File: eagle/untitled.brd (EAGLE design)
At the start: 50 x 50 mm, 39 parts, among them J1 JTAG, Q1 16MHz, U1 MMA3202KEG

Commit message: Update eagle files.
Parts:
- added D10, D11, D12: DIODE, gipi:1206
- C1, C2, C3, C4, C5: device capacitor-wima:C2.5-2 -> SparkFun-Capacitors:1206
- moved GOLD_ORB_SM1 28.6 mm to (31.1, 56.5), flipped to the bottom
- moved C3 13.6 mm to (45.7, 78.1), turned to 0 degrees
- moved C5 10.0 mm to (38.7, 78.1), turned to 180 degrees
- moved JP5 8.28 mm to (5.08, 61.0)
- moved G1 5.46 mm to (8.89, 45.7), flipped to the bottom, turned to 0 degrees
- moved R1 5.08 mm to (12.7, 67.3)
- moved C6 1.91 mm to (12.7, 64.8)
- moved R2 0.63 mm to (12.7, 69.8)
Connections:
- new net N$32: D10.P$1, JP2.VBUS
- new net N$33: D11.P$1, G1.+@1, G1.+@2
- new net N$34: D12.P$1, JP5.2
- net N$28: now also D10.P$2, D11.P$2; no longer G1.+@1, G1.+@2, JP2.VBUS
- net VCC1: now also D12.P$2; no longer JP5.2
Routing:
- net VCC2: track 28.6 -> 59.3 mm, vias 2 -> 0
- net N$17: track 45.4 -> 75.8 mm, vias 2 -> 1
- net N$33: track 0.00 -> 23.4 mm, vias 0 -> 1
- net PD6: track 53.4 -> 34.4 mm, vias 1 -> 2
- net N$28: track 60.9 -> 46.5 mm
- net GND-ISO: track 75.4 -> 88.5 mm, vias 4 -> 9
- net N$11: track 11.0 -> 22.0 mm, vias 1 -> 0
- net PC7: track 63.0 -> 73.3 mm, vias 2 -> 1
- net PB6: track 67.9 -> 77.5 mm, vias 2 -> 1
- net N$13: track 5.90 -> 14.5 mm
- net N$12: track 9.19 -> 17.7 mm
- net N$5: track 16.7 -> 9.69 mm, vias 2 -> 0
- net N$34: track 0.00 -> 5.99 mm
- net N$32: track 0.00 -> 5.18 mm
- net N$6: track 15.3 -> 10.6 mm, vias 2 -> 0
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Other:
- board text added: "!RST"
- board text added: "GND"
- board text added: "PB1"
- board text added: "PB2"
- board text added: "PB3"
- board text added: "VCC"

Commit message: Update board layout.
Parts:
- added D9: (no value), SparkFun-LED:LED-1206
- added JP3: (no value), SparkFun-Connectors:1X04
- added R14: (no value), SparkFun-Passives:1206
- moved SJ1 2.01 mm to (29.8, 75.6)
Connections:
- new net N$18: D9.A, R14.2
- new net PB0: JP3.3, U$1.8
- new net PD0: JP3.1, U$1.18
- new net PD1: JP3.2, U$1.19
- new net PE6: JP3.4, U$1.1
- net GND-ISO: now also D9.C
- net N$28: now also R14.1
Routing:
- net PE6: track 0.00 -> 29.3 mm, vias 0 -> 1
- net PB0: track 0.00 -> 28.8 mm, vias 0 -> 1
- net PD0: track 0.00 -> 28.1 mm, vias 0 -> 1
- net PD1: track 0.00 -> 22.6 mm, vias 0 -> 1
- net GND-ISO: track 88.5 -> 67.3 mm, vias 9 -> 10
- net VCC1: track 76.5 -> 91.7 mm
- net VCC2: track 59.3 -> 48.0 mm
- net X: track 66.1 -> 70.5 mm, vias 0 -> 1
- net N$18: track 0.00 -> 4.38 mm
- net N$6: track 10.6 -> 13.3 mm
- net N$28: track 46.5 -> 49.3 mm
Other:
- board text added: "!CTS"
- board text added: "!RTS"
- board text added: "ACC"
- board text added: "ATMEGA"
- board text added: "PB0"
- board text added: "PD0"
- board text added: "PD1"
- board text added: "PE6"
- board text added: "PWR"
- board text added: "RX"
- board text added: "TX"

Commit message: Update eagle.
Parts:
- added U$2: KITTEN, gipi:KITTEN
- G1: device battery:10MM_SM_COIN_CELL_CLIP -> SparkFun-Electromechanical:BATTCOM_20MM_PTH
- moved G1 6.17 mm to (15.0, 45.1)
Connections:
- net GND-ISO: now also G1.1; no longer G1.-
- net N$33: now also G1.2; no longer G1.+@1, G1.+@2
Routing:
- net GND-ISO: track 67.3 -> 72.9 mm
- net N$33: track 23.4 -> 26.6 mm
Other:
- board text added: "+"
- board text added: "-"
- board text added: "github.com/gipi/pov-project"
- board text removed: "UP ->"
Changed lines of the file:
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@@
 <setting verticaltext="up"/>
 </settings>
-<grid distance="25" unitdist="mil" unit="mil" style="lines" multiple="1" display="no" altdistance="5" altunitdist="mil" altunit="mil"/>
+<grid distance="0.001667" unitdist="inch" unit="inch" style="lines" multiple="1" display="yes" altdistance="5" altunitdist="mil" altunit="mil"/>
 <layers>
 <layer number="1" name="Top" color="4" fill="1" visible="yes" active="yes"/>
@@
 <layer number="20" name="Dimension" color="15" fill="1" visible="yes" active="yes"/>
 <layer number="21" name="tPlace" color="7" fill="1" visible="yes" active="yes"/>
-<layer number="22" name="bPlace" color="7" fill="1" visible="yes" active="yes"/>
+<layer number="22" name="bPlace" color="15" fill="1" visible="yes" active="yes"/>
 <layer number="23" name="tOrigins" color="15" fill="1" visible="yes" active="yes"/>
 <layer number="24" name="bOrigins" color="15" fill="1" visible="yes" active="yes"/>
@@
 <wire x1="50" y1="80" x2="0" y2="80" width="0" layer="20"/>
 <wire x1="0" y1="80" x2="0" y2="30" width="0" layer="20"/>
-<text x="41.91" y="77.47" size="1.778" layer="21">UP -&gt;</text>
 <text x="44.704" y="31.369" size="0.8128" layer="21" font="vector">PD4</text>
 <text x="44.704" y="33.909" size="0.8128" layer="21" font="vector">PD6</text>
@@
 <text x="45.339" y="61.976" size="0.8128" layer="21" font="vector" ratio="10">PD1</text>
 <text x="49.149" y="62.484" size="0.8128" layer="21" font="vector" ratio="10" rot="R90">PD0</text>
+<text x="5.715" y="45.466" size="1.778" layer="21">-</text>
+<text x="20.955" y="45.085" size="1.778" layer="21">+</text>
+<circle x="6.35" y="46.355" radius="1.27" width="0.3048" layer="21"/>
+<text x="49.582246875" y="66.942384375" size="2.1844" layer="22" font="vector" rot="MR0">github.com/gipi/pov-project</text>
 </plain>
 <attributes>
@@
 <element name="C2" library="SparkFun-Capacitors" package="1206" value="" x="19.05" y="43.815"/>
 <element name="U1" library="gipi" package="SOIC20" value="MMA3202KEG" x="40.64" y="69.85"/>
-<element name="G1" library="battery" package="10MM_SM_COIN_CELL_CLIP" value="BAT" x="8.89" y="45.72" smashed="yes" rot="MR0">
-<attribute name="NAME" x="2.85375" y="48.44251875" size="1.27" layer="26" font="vector" rot="MR0"/>
-<attribute name="VALUE" x="13.37255" y="39.28065" size="1.27" layer="28" font="vector" rot="MR0"/>
+<element name="G1" library="SparkFun-Electromechanical" package="BATTCOM_20MM_PTH" value="BAT" x="15.025" y="45.085" smashed="yes" rot="MR0">
+<attribute name="NAME" x="8.98875" y="47.80751875" size="1.27" layer="26" font="vector" rot="MR0"/>
+<attribute name="VALUE" x="19.50755" y="38.64565" size="1.27" layer="28" font="vector" rot="MR0"/>
 </element>
 <element name="C3" library="SparkFun-Capacitors" package="1206" value="" x="45.72" y="78.105" smashed="yes">
-<attribute name="NAME" x="42.799" y="77.089" size="1.27" layer="25" ratio="10" rot="R90"/>
+<attribute name="NAME" x="49.53" y="77.089" size="1.27" layer="25" ratio="10" rot="R90"/>
 <attribute name="VALUE" x="44.069" y="75.311" size="1.27" layer="27" ratio="10"/>
 </element>
@@
 <element name="R14" library="SparkFun-Passives" package="1206" value="" x="18.415" y="69.85"/>
 <element name="JP3" library="SparkFun-Connectors" package="1X04" value="" x="48.26" y="60.325" rot="R180"/>
+<element name="U$2" library="gipi" package="KITTEN" value="KITTEN" x="47.4228125" y="32.7302125" rot="MR0"/>
 </elements>
 <signals>
@@
 <contactref element="C1" pad="1"/>
 <contactref element="C2" pad="1"/>
-<contactref element="G1" pad="-"/>
+<contactref element="G1" pad="1"/>
 <contactref element="C5" pad="1"/>
 <contactref element="C4" pad="1"/>
@@
 <wire x1="8.8392" y1="54.5592" x2="8.8392" y2="45.72" width="0.1524" layer="16"/>
 <wire x1="7.62" y1="55.7784" x2="8.8392" y2="54.5592" width="0.1524" layer="16"/>
-<wire x1="8.8392" y1="45.72" x2="8.89" y2="45.72" width="0.1524" layer="16"/>
+<wire x1="8.8392" y1="45.72" x2="3.175" y2="45.085" width="0.1524" layer="16"/>
 <wire x1="7.62" y1="55.7784" x2="7.62" y2="55.88" width="0.1524" layer="16"/>
 <wire x1="44.5008" y1="78.1812" x2="44.32" y2="78.105" width="0.1524" layer="1"/>
@@
 <contactref element="R11" pad="2"/>
 <wire x1="33.8328" y1="59.436" x2="33.2232" y2="59.436" width="0.1524" layer="1"/>
-<wire x1="38.5572" y1="54.7116" x2="33.8328" y2="59.436" width="0.1524" layer="1"/>
-<wire x1="38.5572" y1="54.4068" x2="38.5572" y2="54.7116" width="0.1524" layer="1"/>
-<wire x1="39.3192" y1="53.6448" x2="38.5572" y2="54.4068" width="0.1524" layer="16"/>
+<wire x1="37.2872" y1="55.9816" x2="33.8328" y2="59.436" width="0.1524" layer="1"/>
+<wire x1="37.9222" y1="55.2958" x2="37.2872" y2="55.9816" width="0.1524" layer="1"/>
+<wire x1="39.3192" y1="53.6448" x2="37.9222" y2="55.2958" width="0.1524" layer="16"/>
 <wire x1="39.9288" y1="53.0352" x2="39.3192" y2="53.6448" width="0.1524" layer="1"/>
 <wire x1="39.9288" y1="44.196" x2="39.9288" y2="53.0352" width="0.1524" layer="1"/>
@@
 <wire x1="39.9288" y1="44.196" x2="41.148" y2="44.196" width="0.1524" layer="1"/>
 <wire x1="47.5488" y1="36.8808" x2="48.26" y2="36.83" width="0.1524" layer="1"/>
-<via x="38.5572" y="54.4068" extent="1-16" drill="0.3048"/>
+<via x="37.9222" y="55.2958" extent="1-16" drill="0.3048"/>
 <via x="39.3192" y="53.6448" extent="1-16" drill="0.3048"/>
 </signal>
@@
 <wire x1="33.9852" y1="60.198" x2="33.2232" y2="60.198" width="0.1524" layer="1"/>
 <wire x1="39.1668" y1="55.0164" x2="33.9852" y2="60.198" width="0.1524" layer="1"/>
-<wire x1="39.9288" y1="54.2544" x2="39.1668" y2="55.0164" width="0.1524" layer="16"/>
-<wire x1="39.9288" y1="53.4924" x2="39.9288" y2="54.2544" width="0.1524" layer="1"/>
-<wire x1="45.72" y1="47.7012" x2="39.9288" y2="53.4924" width="0.1524" layer="1"/>
+<wire x1="40.5638" y1="53.6194" x2="39.1668" y2="55.0164" width="0.1524" layer="16"/>
+<wire x1="40.5638" y1="52.8574" x2="40.5638" y2="53.6194" width="0.1524" layer="1"/>
+<wire x1="45.72" y1="47.7012" x2="40.5638" y2="52.8574" width="0.1524" layer="1"/>
 <wire x1="45.72" y1="41.3004" x2="45.72" y2="47.7012" width="0.1524" layer="1"/>
 <wire x1="47.5488" y1="39.4716" x2="45.72" y2="41.3004" width="0.1524" layer="1"/>
@@
 <wire x1="37.338" y1="42.0624" x2="32.1564" y2="42.0624" width="0.1524" layer="1"/>
 <wire x1="39.3192" y1="44.0436" x2="37.338" y2="42.0624" width="0.1524" layer="1"/>
-<wire x1="39.3192" y1="52.8828" x2="39.3192" y2="44.0436" width="0.1524" layer="1"/>
-<wire x1="39.9288" y1="53.4924" x2="39.3192" y2="52.8828" width="0.1524" layer="16"/>
-<wire x1="39.9288" y1="54.2544" x2="39.9288" y2="53.4924" width="0.1524" layer="16"/>
+<wire x1="39.3192" y1="51.6128" x2="39.3192" y2="44.0436" width="0.1524" layer="1"/>
+<wire x1="39.9288" y1="53.4924" x2="39.3192" y2="51.6128" width="0.1524" layer="16"/>
+<wire x1="40.5638" y1="53.6194" x2="39.9288" y2="53.4924" width="0.1524" layer="16"/>
 <wire x1="26.0604" y1="40.2336" x2="26.035" y2="40.135" width="0.1524" layer="1"/>
 <via x="39.1668" y="55.0164" extent="1-16" drill="0.3048"/>
-<via x="39.9288" y="54.2544" extent="1-16" drill="0.3048"/>
-<via x="39.3192" y="52.8828" extent="1-16" drill="0.3048"/>
+<via x="40.5638" y="53.6194" extent="1-16" drill="0.3048"/>
+<via x="39.3192" y="51.6128" extent="1-16" drill="0.3048"/>
 </signal>
 <signal name="PB5">
@@
 </signal>
 <signal name="N$33">
-<contactref element="G1" pad="+@2"/>
-<contactref element="G1" pad="+@1"/>
+<contactref element="G1" pad="2"/>
 <contactref element="D11" pad="P$1"/>
-<wire x1="4.7244" y1="48.006" x2="4.7244" y2="51.9684" width="0.1524" layer="1"/>
-<wire x1="2.4384" y1="45.72" x2="3.5052" y2="46.7868" width="0.1524" layer="16"/>
-<wire x1="3.5052" y1="46.7868" x2="4.7244" y2="48.006" width="0.1524" layer="16"/>
-<wire x1="4.7244" y1="51.9684" x2="4.8514" y2="52.07" width="0.1524" layer="1"/>
-<wire x1="2.4384" y1="45.72" x2="2.29" y2="45.72" width="0.1524" layer="16"/>
-<wire x1="13.2588" y1="45.72" x2="15.49" y2="45.72" width="0.1524" layer="16"/>
-<wire x1="10.9728" y1="43.434" x2="13.2588" y2="45.72" width="0.1524" layer="16"/>
-<wire x1="6.858" y1="43.434" x2="10.9728" y2="43.434" width="0.1524" layer="16"/>
-<wire x1="3.5052" y1="46.7868" x2="6.858" y2="43.434" width="0.1524" layer="16"/>
-<wire x1="3.5052" y1="46.7868" x2="2.29" y2="45.72" width="0.1524" layer="16"/>
-<via x="4.7244" y="48.006" extent="1-16" drill="0.3048"/>
+<wire x1="4.8514" y1="52.07" x2="4.8514" y2="47.8536" width="0.3048" layer="1"/>
+<wire x1="4.8514" y1="47.8536" x2="5.08" y2="43.815" width="0.3048" layer="1"/>
+<via x="5.08" y="43.815" extent="1-16" drill="0.3048"/>
+<wire x1="5.08" y1="43.815" x2="12.7" y2="45.72" width="0.3048" layer="16"/>
+<wire x1="12.7" y1="45.72" x2="23.175" y2="45.085" width="0.3048" layer="16"/>
 </signal>
 <signal name="N$34">
@@
 <wire x1="31.75" y1="55.245" x2="40.005" y2="58.42" width="0.1524" layer="16"/>
 </signal>
+<signal name="N$31">
+</signal>
 </signals>

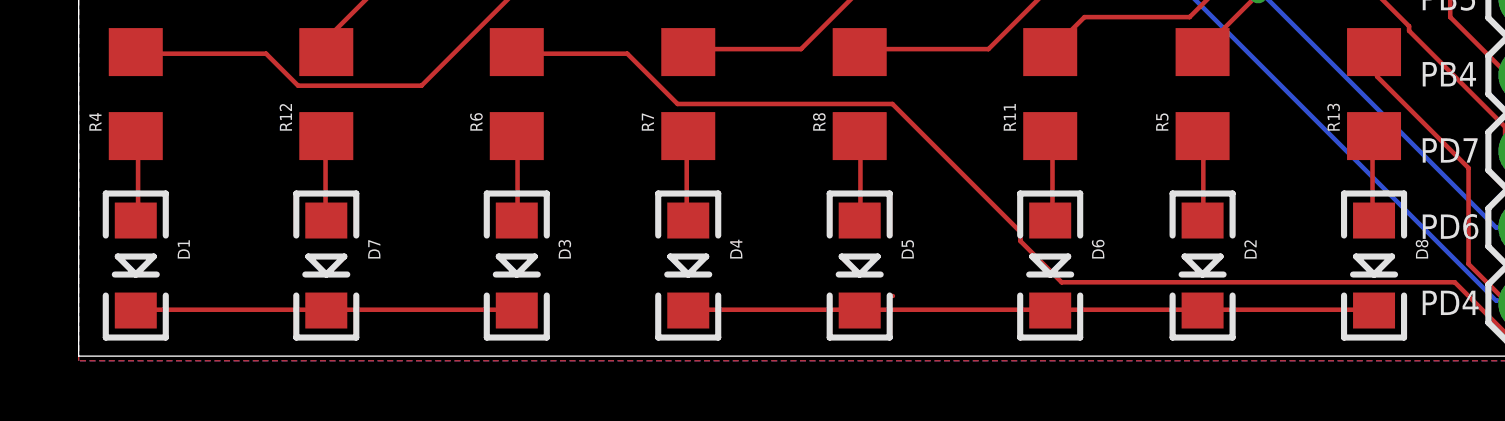
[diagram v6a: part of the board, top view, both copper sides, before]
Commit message: Update some component values.
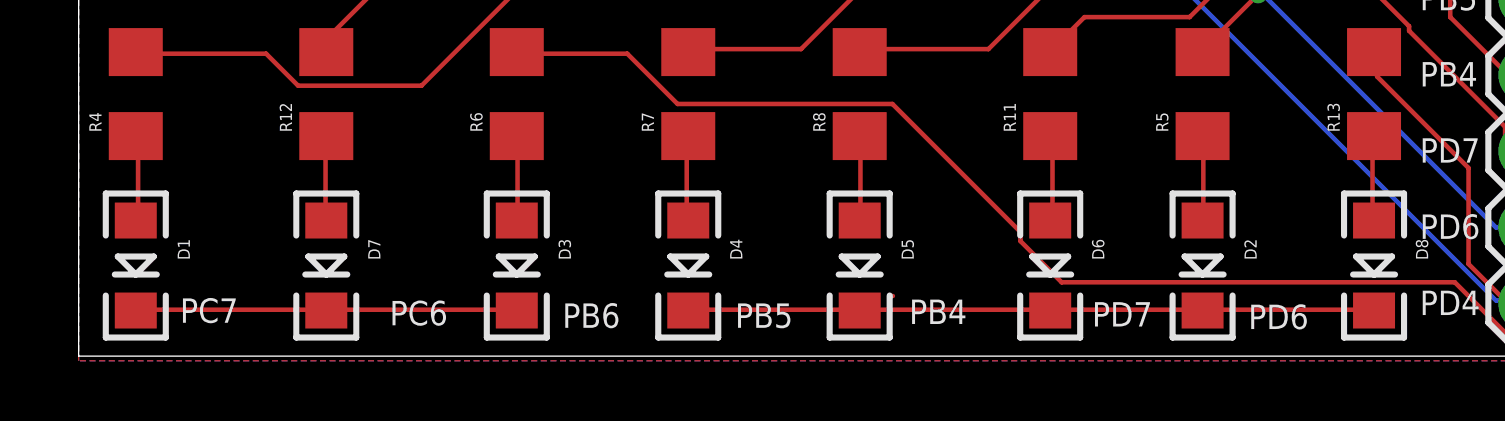
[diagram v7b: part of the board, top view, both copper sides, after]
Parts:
- C1, C2: value (none) -> 22pF
- C3: value (none) -> 0.1uF
- C4, C5: value (none) -> 10pF
- R1, R2: value (none) -> 22
- R10, R9: value 10k -> 1k
- R14: value (none) -> 1k
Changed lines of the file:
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@@
 <circle x="6.35" y="46.355" radius="1.27" width="0.3048" layer="21"/>
 <text x="49.582246875" y="66.942384375" size="2.1844" layer="22" font="vector" rot="MR0">github.com/gipi/pov-project</text>
+<text x="3.378403125" y="31.11139375" size="0.8128" layer="21" font="vector">PC7</text>
+<text x="10.3648" y="31.02721875" size="0.8128" layer="21" font="vector">PC6</text>
+<text x="16.123284375" y="30.943040625" size="0.8128" layer="21" font="vector">PB6</text>
+<text x="21.88176875" y="30.94355" size="0.8128" layer="21" font="vector">PB5</text>
+<text x="27.682596875" y="31.07108125" size="0.8128" layer="21" font="vector">PB4</text>
+<text x="33.779815625" y="30.98690625" size="0.8128" layer="21" font="vector">PD7</text>
+<text x="38.98785625" y="30.90273125" size="0.8128" layer="21" font="vector">PD6</text>
 </plain>
 <attributes>
@@
 <attribute name="PROD_ID" value="IC-11161" x="27.305" y="60.325" size="1.778" layer="27" display="off"/>
 </element>
-<element name="R1" library="SparkFun-Passives" package="1206" value="" x="12.7" y="67.31"/>
-<element name="R2" library="SparkFun-Passives" package="1206" value="" x="12.7" y="69.85"/>
+<element name="R1" library="SparkFun-Passives" package="1206" value="22" x="12.7" y="67.31"/>
+<element name="R2" library="SparkFun-Passives" package="1206" value="22" x="12.7" y="69.85"/>
 <element name="S1" library="SparkFun-Retired" package="TACTILE-SWITCH-SMD" value="RESET" x="12.7" y="76.835" smashed="yes">
 <attribute name="PROD_ID" value="SWCH-08247" x="12.7" y="76.835" size="1.778" layer="27" display="off"/>
@@
 <attribute name="NAME" x="25.4" y="50.038" size="1.27" layer="25" ratio="10" rot="R180"/>
 </element>
-<element name="C1" library="SparkFun-Capacitors" package="1206" value="" x="27.94" y="43.815" smashed="yes" rot="R180">
+<element name="C1" library="SparkFun-Capacitors" package="1206" value="22pF" x="27.94" y="43.815" smashed="yes" rot="R180">
 <attribute name="NAME" x="29.591" y="46.736" size="1.27" layer="25" ratio="10" rot="R180"/>
 <attribute name="VALUE" x="29.591" y="46.609" size="1.27" layer="27" ratio="10" rot="R180"/>
 </element>
-<element name="C2" library="SparkFun-Capacitors" package="1206" value="" x="19.05" y="43.815"/>
+<element name="C2" library="SparkFun-Capacitors" package="1206" value="22pF" x="19.05" y="43.815"/>
 <element name="U1" library="gipi" package="SOIC20" value="MMA3202KEG" x="40.64" y="69.85"/>
 <element name="G1" library="SparkFun-Electromechanical" package="BATTCOM_20MM_PTH" value="BAT" x="15.025" y="45.085" smashed="yes" rot="MR0">
@@
 <attribute name="VALUE" x="19.50755" y="38.64565" size="1.27" layer="28" font="vector" rot="MR0"/>
 </element>
-<element name="C3" library="SparkFun-Capacitors" package="1206" value="" x="45.72" y="78.105" smashed="yes">
+<element name="C3" library="SparkFun-Capacitors" package="1206" value="0.1uF" x="45.72" y="78.105" smashed="yes">
 <attribute name="NAME" x="49.53" y="77.089" size="1.27" layer="25" ratio="10" rot="R90"/>
 <attribute name="VALUE" x="44.069" y="75.311" size="1.27" layer="27" ratio="10"/>
 </element>
 <element name="SJ1" library="SparkFun-Retired" package="SJ_3_PASTE2&amp;3" value="" x="29.845" y="75.565" rot="R180"/>
-<element name="R9" library="SparkFun-Passives" package="1206" value="10k" x="33.02" y="76.2" rot="R270"/>
-<element name="R10" library="SparkFun-Passives" package="1206" value="10k" x="24.13" y="71.12" rot="R180"/>
-<element name="C4" library="SparkFun-Capacitors" package="1206" value="" x="29.845" y="71.12" rot="R180"/>
-<element name="C5" library="SparkFun-Capacitors" package="1206" value="" x="38.735" y="78.105" smashed="yes" rot="R180">
+<element name="R9" library="SparkFun-Passives" package="1206" value="1k" x="33.02" y="76.2" rot="R270"/>
+<element name="R10" library="SparkFun-Passives" package="1206" value="1k" x="24.13" y="71.12" rot="R180"/>
+<element name="C4" library="SparkFun-Capacitors" package="1206" value="10pF" x="29.845" y="71.12" rot="R180"/>
+<element name="C5" library="SparkFun-Capacitors" package="1206" value="10pF" x="38.735" y="78.105" smashed="yes" rot="R180">
 <attribute name="NAME" x="41.529" y="79.375" size="1.27" layer="25" ratio="10" rot="R270"/>
 <attribute name="VALUE" x="40.386" y="80.899" size="1.27" layer="27" ratio="10" rot="R180"/>
@@
 <element name="D12" library="gipi" package="1206" value="DIODE" x="14.605" y="62.23"/>
 <element name="D9" library="SparkFun-LED" package="LED-1206" value="" x="18.415" y="66.675"/>
-<element name="R14" library="SparkFun-Passives" package="1206" value="" x="18.415" y="69.85"/>
+<element name="R14" library="SparkFun-Passives" package="1206" value="1k" x="18.415" y="69.85"/>
 <element name="JP3" library="SparkFun-Connectors" package="1X04" value="" x="48.26" y="60.325" rot="R180"/>
 <element name="U$2" library="gipi" package="KITTEN" value="KITTEN" x="47.4228125" y="32.7302125" rot="MR0"/>
